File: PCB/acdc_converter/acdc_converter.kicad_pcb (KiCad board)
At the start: 2 copper layers, 150 x 90 mm, 64 parts, among them J1 MAINS L N PE, J2 9V OUT, K1 G6K-2F-Y DC12, K2 G6K-2F-Y DC12, Q1 2N7002, U1 LM317, U2 LM317, U3 L78L12, U4 CD4060B, U5 LT3045

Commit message: Route the two-bucket PSU board: fully connected, DRC clean but one thermal
Freerouting 1.9 in batch mode (2.1 never saved its session). Grounds
are routed on this board because the relays switch bucket current in
the unpoured area; mains nets 1.0 mm / 2.0 mm, current paths 0.6 mm;
hand-routed 1 mm PE rail on the left edge, GND_C-PE bond at the PE
hole; only the two mains-side holes are PE, the receiver-side holes
are unplated. Plain exposed-pad footprints (the thermal-via variants
need 0.2 mm drills). Newava S2208x redrawn as a 4-pin part (windings
1-2 / 3-4 per the DCR spec) with slotted pins 2/4 fitting either pitch.

Co-Authored-By: Claude Opus 5.5 <noreply@anthropic.com>
Claude-Session: https://claude.ai/code/session_01RsM1DhHhY1tSr2aHjVygSC
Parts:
- H2, H4: value M3 PE -> M3; footprint MountingHole:MountingHole_3.2mm_M3_Pad_Via -> MountingHole:MountingHole_3.2mm_M3
- U5: footprint Package_SO:MSOP-12-1EP_3x4.039mm_P0.65mm_EP1.651x2.845mm_ThermalVias -> Package_SO:MSOP-12-1EP_3x4.039mm_P0.65mm_EP1.651x2.845mm
- moved R1 61.4 mm to (63.0, 54.5), turned to 180 degrees
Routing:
- net GND_C: track 0.00 -> 210.5 mm, vias 0 -> 57
- net GND: track 0.00 -> 119.0 mm, vias 0 -> 60
- net PE: track 0.00 -> 107.6 mm
- net +12V_C: track 0.00 -> 101.2 mm, vias 0 -> 4
- net +15V_C: track 0.00 -> 84.2 mm, vias 0 -> 2
- net COIL_N: track 0.00 -> 70.6 mm
- net LOAD_P: track 0.00 -> 56.9 mm
- net B_P: track 0.00 -> 51.4 mm, vias 0 -> 1
- net AC_N: track 0.00 -> 48.9 mm
- net CHG_A: track 0.00 -> 40.8 mm
- net AC_L: track 0.00 -> 39.8 mm
- net SET: track 0.00 -> 39.8 mm, vias 0 -> 2
- net LOAD_A: track 0.00 -> 38.3 mm
- net VREG: track 0.00 -> 37.3 mm
- net CC_OUT: track 0.00 -> 36.5 mm
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- added copper zone on B.Cu, net GND
- added copper zone on F.Cu, net GND
- added copper zone on B.Cu, net GND_C
- added copper zone on F.Cu, net GND_C

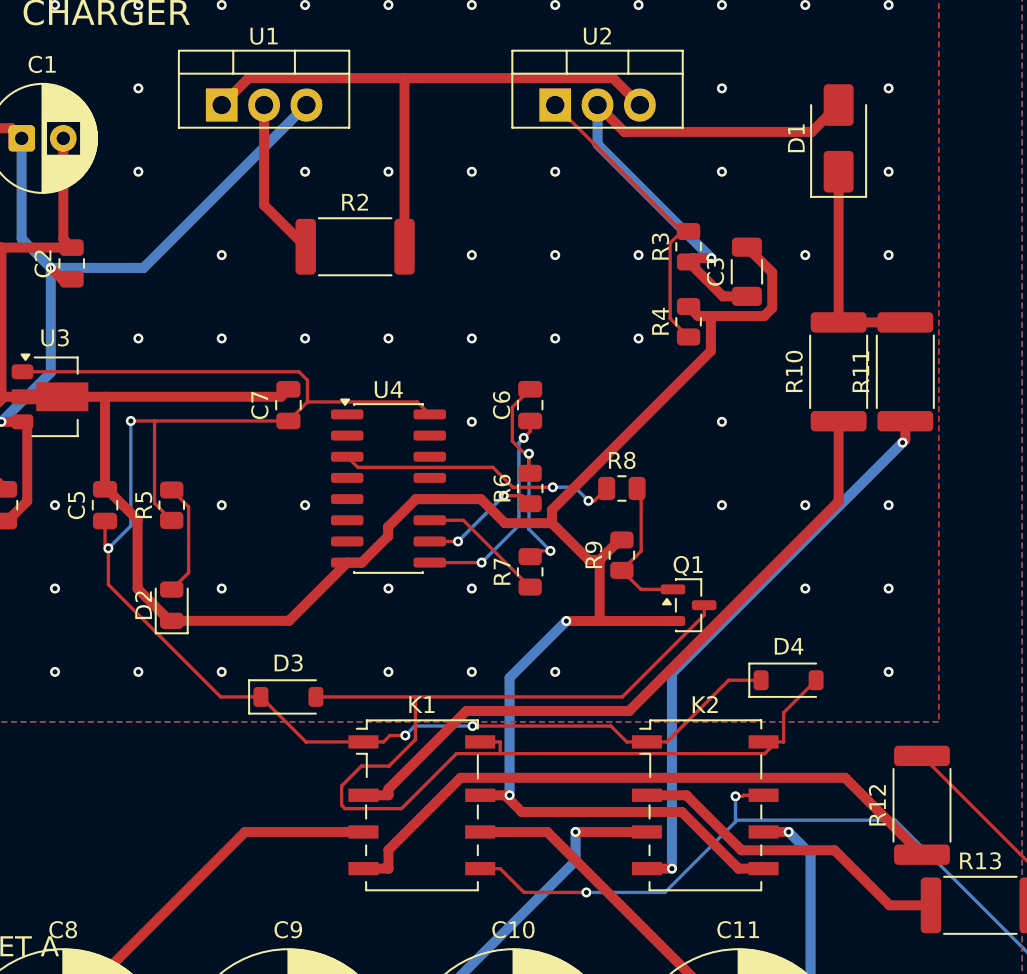
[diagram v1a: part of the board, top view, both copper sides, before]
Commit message: PSU board re-routed with the simulation fixes; fab outputs
Gerbers + drill (JLCPCB zip), pick-and-place, BOM, schematic and
assembly PDFs, 3D render in PCB/acdc_converter/fab/. DRC: fully
connected, one starved thermal relief on C4 (benign).

Co-Authored-By: Claude Opus 5.5 <noreply@anthropic.com>
Claude-Session: https://claude.ai/code/session_01RsM1DhHhY1tSr2aHjVygSC
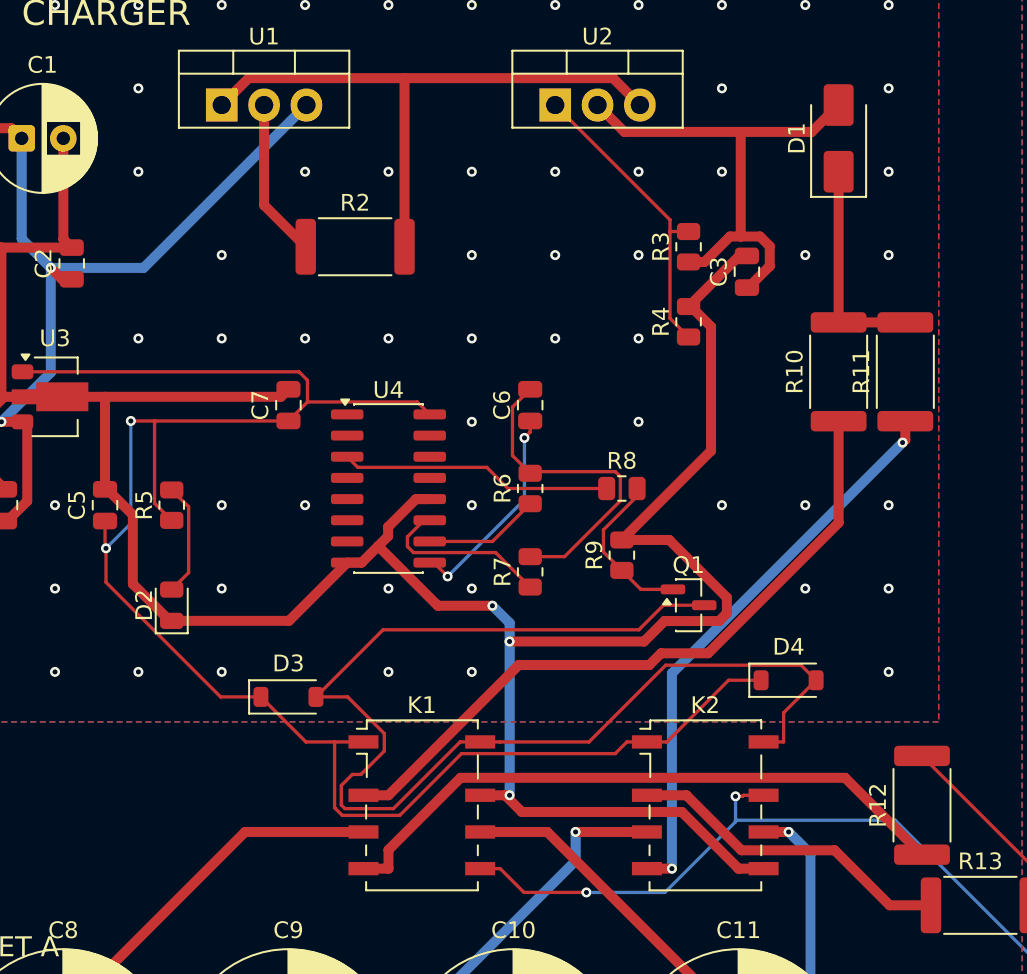
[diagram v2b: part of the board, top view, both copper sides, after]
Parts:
- C3: value 10u -> 100n; footprint Capacitor_SMD:C_1206_3216Metric -> Capacitor_SMD:C_0805_2012Metric
- R22: value 84.5k -> 69.8k
- R6: value 160k -> 80.6k
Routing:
- net +12V_C: track 101.2 -> 108.1 mm, vias 4 -> 2
- net OSC_X: track 13.8 -> 19.7 mm, vias 2 -> 0
- net COIL_N: track 70.6 -> 74.4 mm
- net OSC_I: track 7.68 -> 10.7 mm
- net CHG: track 33.6 -> 30.9 mm, vias 1 -> 0
- net GND_C: track 210.5 -> 213.1 mm, vias 57 -> 59
- net GATE: track 9.03 -> 9.74 mm
- net SWAP: track 17.0 -> 16.4 mm, vias 2 -> 0
- net CHG_A: track 40.8 -> 41.4 mm
- net OSC_R: track 7.36 -> 6.96 mm, vias 2 -> 0
